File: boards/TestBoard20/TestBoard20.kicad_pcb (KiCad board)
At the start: 2 copper layers, 37.5 x 87.6 mm, 28 parts, among them J1 Conn_01x04, J10 Conn_01x02, J11 Conn_01x02, J12 Conn_01x20, J13 Conn_01x20, J14 Conn_01x20, J15 Conn_01x20, J2 Conn_01x04, J4 Conn_01x02, J6 Conn_01x20, J7 Conn_01x20, J8 Conn_01x20, J9 Conn_01x20, U1 MCP23017_SS, U2 MCP23017_SS, U3 MCP23017_SS, U4 MCP23017_SS, U5 MCP23017_SS

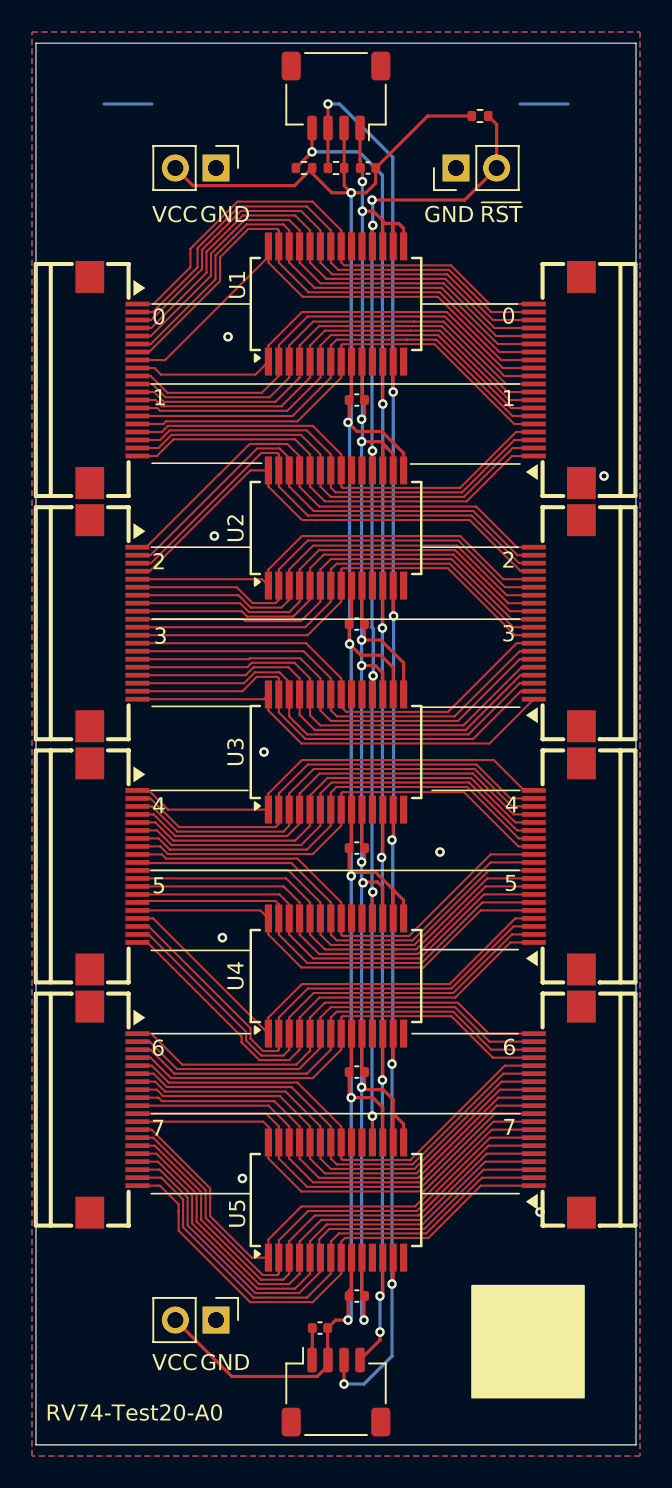
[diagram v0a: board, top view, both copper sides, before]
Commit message: Add 2.5mm mounting holes
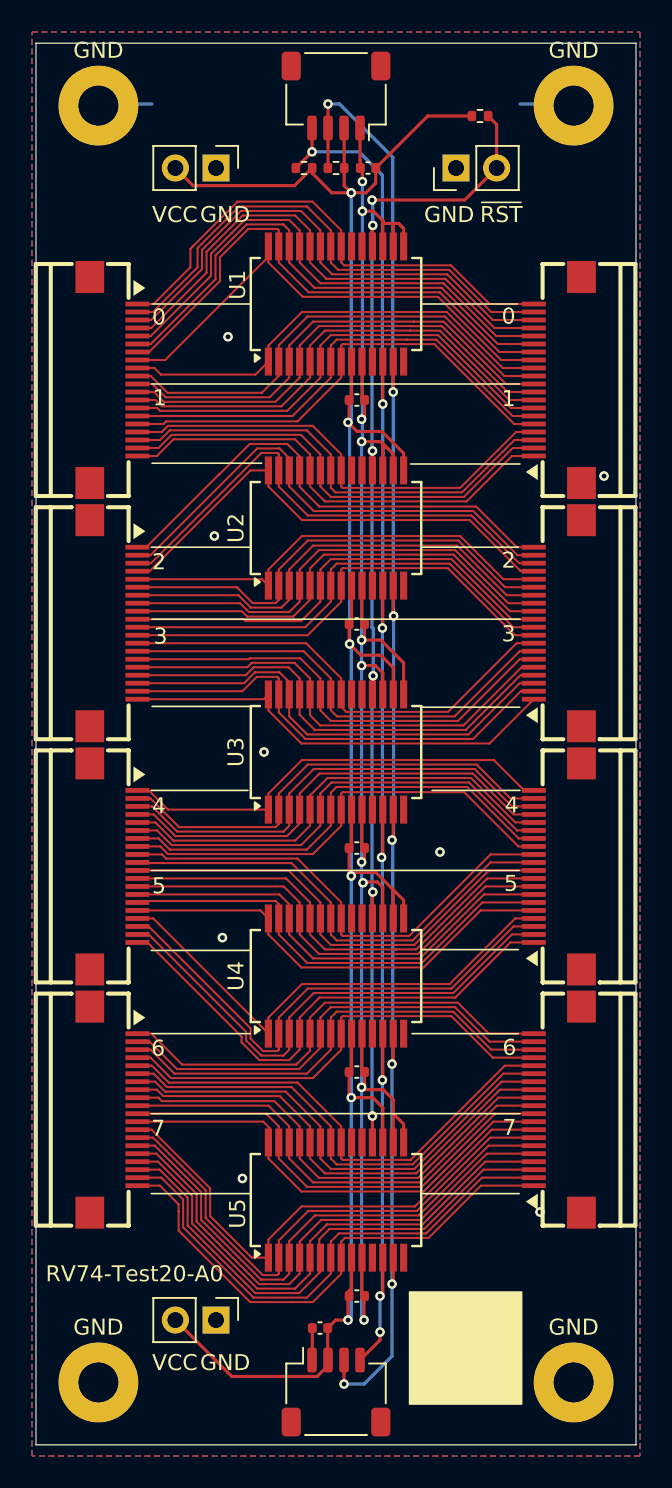
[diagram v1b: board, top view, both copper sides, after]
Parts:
- added GND: MountingHole_2.5mm_Pad, MountingHole:MountingHole_2.5mm_Pad, F.Cu at (104.7, 45.1)
- added GND: MountingHole_2.5mm_Pad, MountingHole:MountingHole_2.5mm_Pad, F.Cu at (104.7, 124.9)
- added GND: MountingHole_2.5mm_Pad, MountingHole:MountingHole_2.5mm_Pad, F.Cu at (134.3, 124.9)
- added GND: MountingHole_2.5mm_Pad, MountingHole:MountingHole_2.5mm_Pad, F.Cu at (134.3, 45.1)

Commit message: Use M2 mounting holes rather than 2.5mm holes
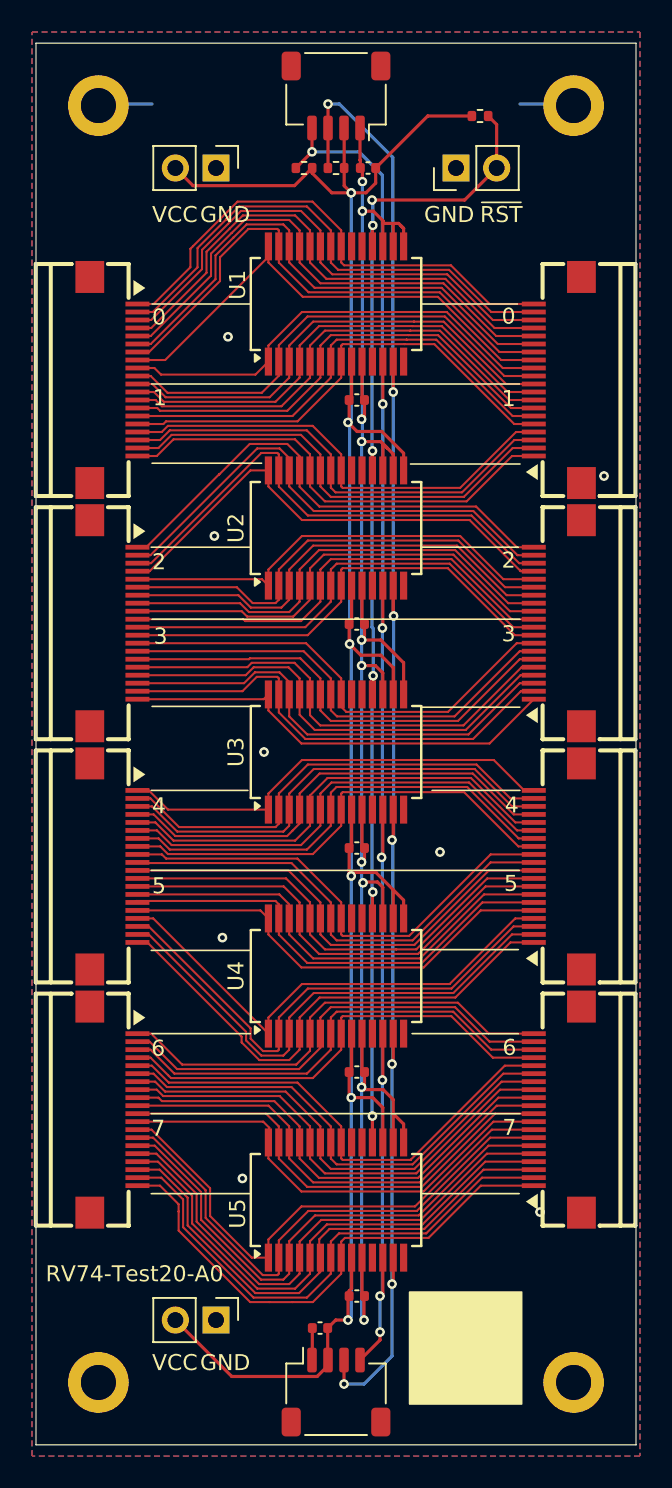
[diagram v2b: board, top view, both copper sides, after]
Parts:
- GND (x4): value MountingHole_2.5mm_Pad -> MountingHole_2.2mm_M2_ISO14580_Pad; footprint MountingHole:MountingHole_2.5mm_Pad -> MountingHole:MountingHole_2.2mm_M2_ISO14580_Pad
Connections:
- GND pad 1: (no net) -> GND (x4)
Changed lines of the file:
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@@
 		)
 	)
-	(footprint "MountingHole:MountingHole_2.5mm_Pad"
+	(footprint "MountingHole:MountingHole_2.2mm_M2_ISO14580_Pad"
 		(layer "F.Cu")
 		(at 104.65 45.1)
-		(descr "Mounting Hole 2.5mm, generated by kicad-footprint-generator mountinghole.py")
-		(tags "mountinghole")
+		(descr "Mounting Hole 2.2mm, M2, generated by kicad-footprint-generator mountinghole.py")
+		(tags "mountinghole M2 ISO14580")
 		(property "Reference" "GND"
-			(at 0 -3.45 0)
+			(at 0 -2.85 0)
 			(layer "F.SilkS")
+			(hide yes)
 			(effects
 				(font
@@
 			)
 		)
-		(property "Value" "MountingHole_2.5mm_Pad"
-			(at 0 3.45 0)
+		(property "Value" "MountingHole_2.2mm_M2_ISO14580_Pad"
+			(at 0 2.85 0)
 			(layer "F.Fab")
 			(effects
@@
 		(fp_circle
 			(center 0 0)
-			(end 2.5 0)
+			(end 1.9 0)
 			(stroke
 				(width 0.15)
@@
 		(fp_circle
 			(center 0 0)
-			(end 2.75 0)
+			(end 2.15 0)
 			(stroke
 				(width 0.05)
@@
 			(effects
 				(font
-					(size 1 1)
-					(thickness 0.15)
+					(size 0.95 0.95)
+					(thickness 0.14)
 				)
 			)
@@
 		(pad "1" thru_hole circle
 			(at 0 0)
-			(size 5 5)
-			(drill 2.5)
+			(size 3.8 3.8)
+			(drill 2.2)
 			(layers "*.Cu" "*.Mask")
 			(remove_unused_layers no)
+			(net 1 "GND")
 			(zone_connect 2)
 		)
@@
 		)
 	)
-	(footprint "MountingHole:MountingHole_2.5mm_Pad"
+	(footprint "MountingHole:MountingHole_2.2mm_M2_ISO14580_Pad"
 		(layer "F.Cu")
 		(at 104.65 124.9)
-		(descr "Mounting Hole 2.5mm, generated by kicad-footprint-generator mountinghole.py")
-		(tags "mountinghole")
+		(descr "Mounting Hole 2.2mm, M2, generated by kicad-footprint-generator mountinghole.py")
+		(tags "mountinghole M2 ISO14580")
 		(property "Reference" "GND"
-			(at 0 -3.45 0)
+			(at 0 -2.85 0)
 			(layer "F.SilkS")
+			(hide yes)
 			(effects
 				(font
@@
 			)
 		)
-		(property "Value" "MountingHole_2.5mm_Pad"
-			(at 0 3.45 0)
+		(property "Value" "MountingHole_2.2mm_M2_ISO14580_Pad"
+			(at 0 2.85 0)
 			(layer "F.Fab")
 			(effects
@@
 		(fp_circle
 			(center 0 0)
-			(end 2.5 0)
+			(end 1.9 0)
 			(stroke
 				(width 0.15)
@@
 		(fp_circle
 			(center 0 0)
-			(end 2.75 0)
+			(end 2.15 0)
 			(stroke
 				(width 0.05)
@@
 			(effects
 				(font
-					(size 1 1)
-					(thickness 0.15)
+					(size 0.95 0.95)
+					(thickness 0.14)
 				)
 			)
@@
 		(pad "1" thru_hole circle
 			(at 0 0)
-			(size 5 5)
-			(drill 2.5)
+			(size 3.8 3.8)
+			(drill 2.2)
 			(layers "*.Cu" "*.Mask")
 			(remove_unused_layers no)
+			(net 1 "GND")
 			(zone_connect 2)
 		)
@@
 		)
 	)
-	(footprint "MountingHole:MountingHole_2.5mm_Pad"
+	(footprint "MountingHole:MountingHole_2.2mm_M2_ISO14580_Pad"
 		(layer "F.Cu")
 		(at 134.35 124.9)
-		(descr "Mounting Hole 2.5mm, generated by kicad-footprint-generator mountinghole.py")
-		(tags "mountinghole")
+		(descr "Mounting Hole 2.2mm, M2, generated by kicad-footprint-generator mountinghole.py")
+		(tags "mountinghole M2 ISO14580")
 		(property "Reference" "GND"
-			(at 0 -3.45 0)
+			(at 0 -2.85 0)
 			(layer "F.SilkS")
+			(hide yes)
 			(effects
 				(font
@@
 			)
 		)
-		(property "Value" "MountingHole_2.5mm_Pad"
-			(at 0 3.45 0)
+		(property "Value" "MountingHole_2.2mm_M2_ISO14580_Pad"
+			(at 0 2.85 0)
 			(layer "F.Fab")
 			(effects
@@
 		(fp_circle
 			(center 0 0)
-			(end 2.5 0)
+			(end 1.9 0)
 			(stroke
 				(width 0.15)
@@
 		(fp_circle
 			(center 0 0)
-			(end 2.75 0)
+			(end 2.15 0)
 			(stroke
 				(width 0.05)
@@
 			(effects
 				(font
-					(size 1 1)
-					(thickness 0.15)
+					(size 0.95 0.95)
+					(thickness 0.14)
 				)
 			)
@@
 		(pad "1" thru_hole circle
 			(at 0 0)
-			(size 5 5)
-			(drill 2.5)
+			(size 3.8 3.8)
+			(drill 2.2)
 			(layers "*.Cu" "*.Mask")
 			(remove_unused_layers no)
+			(net 1 "GND")
 			(zone_connect 2)
 		)
@@
 		(embedded_fonts no)
 	)
-	(footprint "MountingHole:MountingHole_2.5mm_Pad"
+	(footprint "MountingHole:MountingHole_2.2mm_M2_ISO14580_Pad"
 		(layer "F.Cu")
 		(at 134.35 45.1)
-		(descr "Mounting Hole 2.5mm, generated by kicad-footprint-generator mountinghole.py")
-		(tags "mountinghole")
+		(descr "Mounting Hole 2.2mm, M2, generated by kicad-footprint-generator mountinghole.py")
+		(tags "mountinghole M2 ISO14580")
 		(property "Reference" "GND"
-			(at 0 -3.45 0)
+			(at 0 -2.85 0)
 			(layer "F.SilkS")
+			(hide yes)
 			(effects
 				(font
@@
 			)
 		)
-		(property "Value" "MountingHole_2.5mm_Pad"
-			(at 0 3.45 0)
+		(property "Value" "MountingHole_2.2mm_M2_ISO14580_Pad"
+			(at 0 2.85 0)
 			(layer "F.Fab")
 			(effects
@@
 		(fp_circle
 			(center 0 0)
-			(end 2.5 0)
+			(end 1.9 0)
 			(stroke
 				(width 0.15)
@@
 		(fp_circle
 			(center 0 0)
-			(end 2.75 0)
+			(end 2.15 0)
 			(stroke
 				(width 0.05)
@@
 			(effects
 				(font
-					(size 1 1)
-					(thickness 0.15)
+					(size 0.95 0.95)
+					(thickness 0.14)
 				)
 			)
@@
 		(pad "1" thru_hole circle
 			(at 0 0)
-			(size 5 5)
-			(drill 2.5)
+			(size 3.8 3.8)
+			(drill 2.2)
 			(layers "*.Cu" "*.Mask")
 			(remove_unused_layers no)
+			(net 1 "GND")
 			(zone_connect 2)
 		)

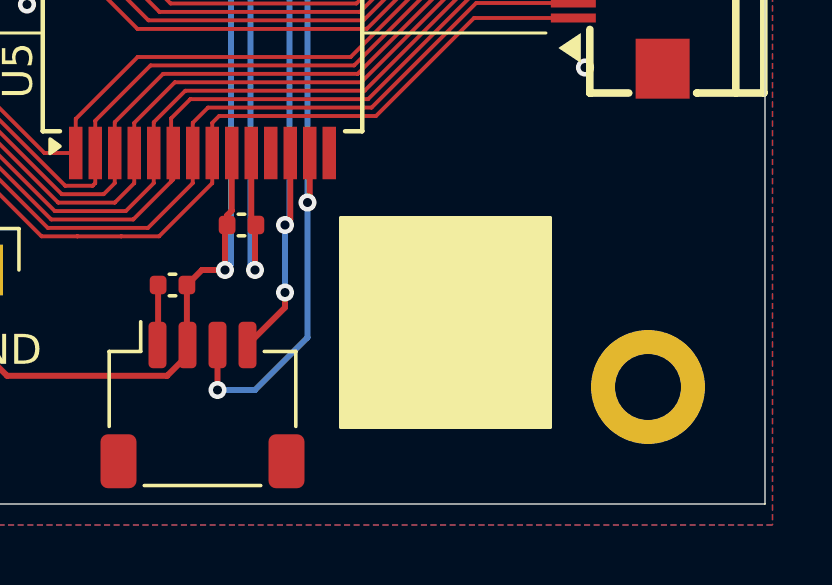
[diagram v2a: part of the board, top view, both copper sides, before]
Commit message: Use a cheaper 20P connector, with more stock. Area for QRCode must be 8x8mm, not 7x7mm
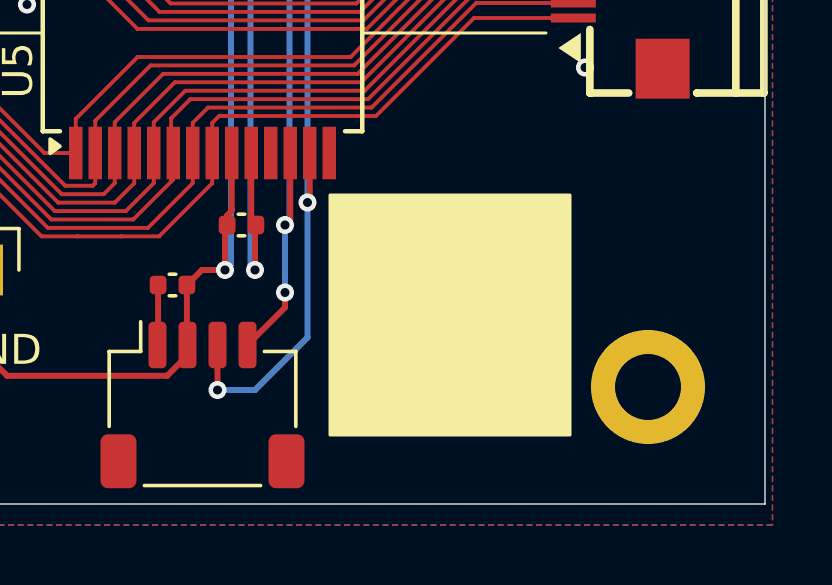
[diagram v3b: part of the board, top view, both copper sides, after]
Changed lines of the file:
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@@
 			)
 		)
-		(property "LCSC" "C2834232"
+		(property "LCSC" "C19267987"
 			(at 0 0 90)
 			(unlocked yes)
@@
 			)
 		)
-		(property "LCSC" "C2834232"
+		(property "LCSC" "C19267987"
 			(at 0 0 270)
 			(unlocked yes)
@@
 			)
 		)
-		(property "LCSC" "C2834232"
+		(property "LCSC" "C19267987"
 			(at 0 0 270)
 			(unlocked yes)
@@
 			)
 		)
-		(property "LCSC" "C2834232"
+		(property "LCSC" "C19267987"
 			(at 0 0 90)
 			(unlocked yes)
@@
 			)
 		)
-		(property "LCSC" "C2834232"
+		(property "LCSC" "C19267987"
 			(at 0 0 270)
 			(unlocked yes)
@@
 			)
 		)
-		(property "LCSC" "C2834232"
+		(property "LCSC" "C19267987"
 			(at 0 0 90)
 			(unlocked yes)
@@
 			)
 		)
-		(property "LCSC" "C2834232"
+		(property "LCSC" "C19267987"
 			(at 0 0 270)
 			(unlocked yes)
@@
 			)
 		)
-		(property "LCSC" "C2834232"
+		(property "LCSC" "C19267987"
 			(at 0 0 90)
 			(unlocked yes)
@@
 	)
 	(gr_rect
-		(start 124.1 119.25)
-		(end 131.1 126.25)
+		(start 123.75 118.5)
+		(end 131.75 126.5)
 		(stroke
 			(width 0.1)
